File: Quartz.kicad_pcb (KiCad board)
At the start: 6 copper layers, 254 x 130 mm, 1244 parts, among them J1 DB37, J2 DB37, J4 Conn_02x10_Odd_Even, J5 PPS IN, J6 WP Jumper, J7 WP Jumper, K1001 EE2-12TNU-L, K101 EE2-12TNU-L, K1101 EE2-12TNU-L, K1201 EE2-12TNU-L, K1301 EE2-12TNU-L, K1401 EE2-12TNU-L, K1501 EE2-12TNU-L, K1601 EE2-12TNU-L, K1701 EE2-12TNU-L, K1801 EE2-12TNU-L, K1901 EE2-12TNU-L, K2001 EE2-12TNU-L, K201 EE2-12TNU-L, K2101 EE2-12TNU-L, K2201 EE2-12TNU-L, K2301 EE2-12TNU-L, K2401 EE2-12TNU-L, K2501 EE2-12TNU-L, K2601 EE2-12TNU-L, K2701 EE2-12TNU-L, K2801 EE2-12TNU-L, K2901 EE2-12TNU-L, K3001 EE2-12TNU-L, K301 EE2-12TNU-L, K3101 EE2-12TNU-L, K3201 EE2-12TNU-L, K401 EE2-12TNU-L, K501 EE2-12TNU-L, K601 EE2-12TNU-L, K701 EE2-12TNU-L, K801 EE2-12TNU-L, K901 EE2-12TNU-L, P1 ASP-134604-01, P2 ASP-134604-01, Q1 FDN335N, Q2 FDN335N, Q3 FDMC510P, U1 AD7768, U10 AD7768, U1001 INA851, U101 INA851, U11 ADR4520, U1101 INA851, U12 ADA4841-1, U1201 INA851, U13 AMC7823, U1301 INA851, U14 MAX4896, U1401 INA851, U15 MAX4896, U1501 INA851, U16 SI5330B-B00205-GM, U1601 INA851, U17 MAX4896, U1701 INA851, U18 MAX4896, U1801 INA851, U19 MAX4896, U1901 INA851, U2 ADR4520, U20 MAX4896, U2001 INA851, U201 INA851, U21 MAX4896, U2101 INA851, U2201 INA851, U23 MAX4896, U2301 INA851, U2401 INA851, U2501 INA851, U26 74AVC4T245, U2601 INA851, U27 AT24C64D, U2701 INA851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

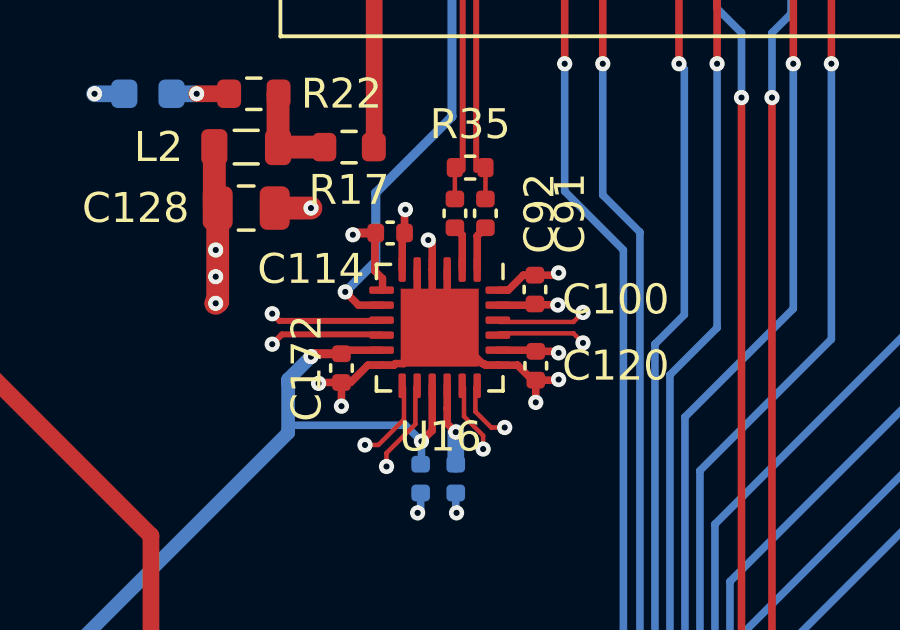
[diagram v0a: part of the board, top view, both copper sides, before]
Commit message: Fixed Grounding under Clk divider
Added Ground Vias Under the Si5330 Chip
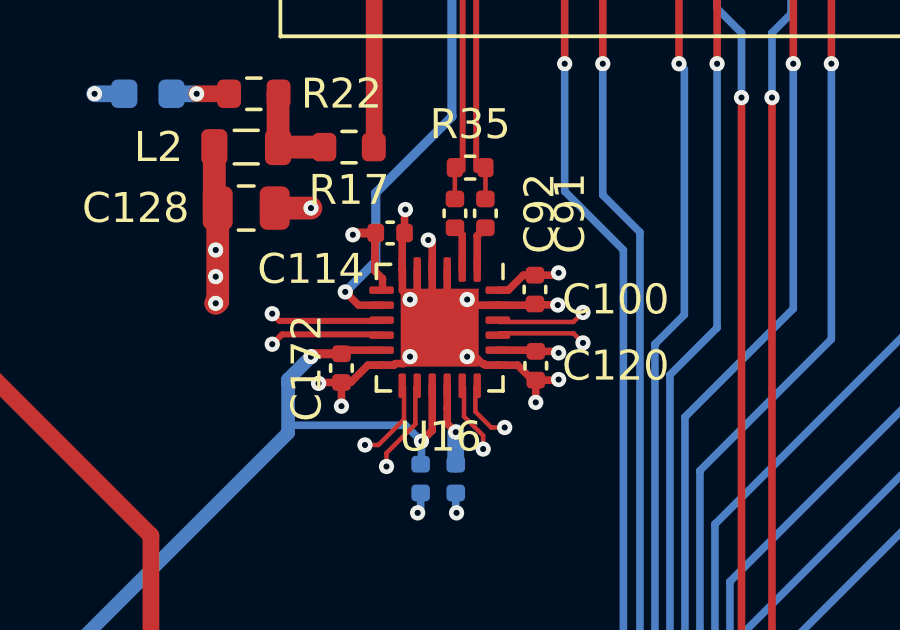
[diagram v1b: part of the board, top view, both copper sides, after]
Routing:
- net GND: track 1050.1 -> 1054.8 mm, vias 669 -> 673
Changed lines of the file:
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@@
 	)
 	(segment
+		(start 221.996 117.2972)
+		(end 221.996 116.6097)
+		(width 0.254)
+		(layer "F.Cu")
+		(net 2)
+	)
+	(segment
 		(start 322.608 129.032)
 		(end 321.818 129.032)
@@
 	)
 	(segment
+		(start 225.1761 117.7898)
+		(end 223.9886 117.7898)
+		(width 0.254)
+		(layer "F.Cu")
+		(net 2)
+	)
+	(segment
 		(start 291.338 180.368)
 		(end 291.338 179.578)
@@
 	)
 	(segment
+		(start 221.996 116.6097)
+		(end 221.9886 116.6023)
+		(width 0.254)
+		(layer "F.Cu")
+		(net 2)
+	)
+	(segment
 		(start 218.539 189.893)
 		(end 218.44 189.992)
@@
 	)
 	(segment
+		(start 223.2386 118.5398)
+		(end 221.996 117.2972)
+		(width 0.254)
+		(layer "F.Cu")
+		(net 2)
+	)
+	(segment
 		(start 246.455 98.313)
 		(end 246.455 97.551001)
@@
 	)
 	(segment
+		(start 223.9886 117.7898)
+		(end 223.2386 118.5398)
+		(width 0.254)
+		(layer "F.Cu")
+		(net 2)
+	)
+	(segment
 		(start 172.645 102.631001)
 		(end 172.645 102.504)
@@
 	)
 	(via
+		(at 222.25 119.507)
+		(size 0.508)
+		(drill 0.2032)
+		(layers "F.Cu" "B.Cu")
+		(free yes)
+		(net 2)
+	)
+	(via
 		(at 108.535501 142.892007)
 		(size 0.508)
@@
 	)
 	(via
+		(at 224.155 117.602)
+		(size 0.508)
+		(drill 0.2032)
+		(layers "F.Cu" "B.Cu")
+		(free yes)
+		(net 2)
+	)
+	(via
 		(at 237.236 156.083)
 		(size 0.5588)
@@
 	)
 	(via
+		(at 224.155 119.507)
+		(size 0.508)
+		(drill 0.2032)
+		(layers "F.Cu" "B.Cu")
+		(free yes)
+		(net 2)
+	)
+	(via
 		(at 93.218 133.223)
 		(size 0.508)
@@
 		(net 2)
 	)
+	(via
+		(at 222.25 117.602)
+		(size 0.508)
+		(drill 0.2032)
+		(layers "F.Cu" "B.Cu")
+		(free yes)
+		(net 2)
+	)
